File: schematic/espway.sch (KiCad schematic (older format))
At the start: 33 parts, among them J1 CONN_01X02, J2 CONN_01X02, J3 Conn_01x05_Male, SW1 SW_Push, U1 LM1117-3.3, U2 ESP-12E, U3 DRV8835, U4 LSM6DS3

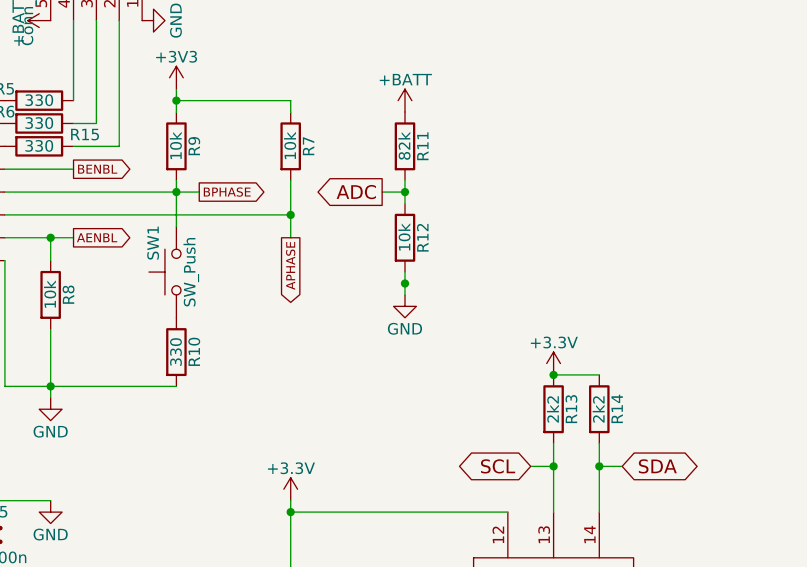
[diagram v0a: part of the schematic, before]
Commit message: Minor PCB track adjustments
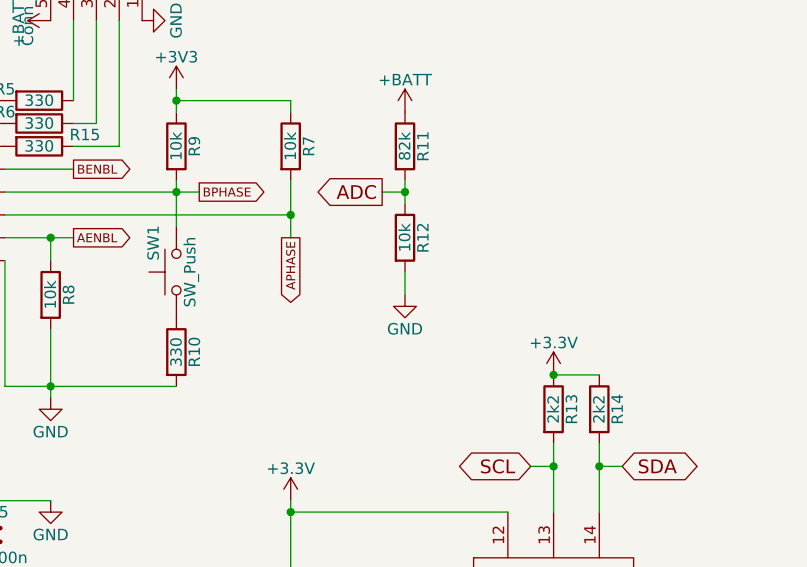
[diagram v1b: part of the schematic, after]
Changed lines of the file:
@@
 Wire Wire Line
 	10200 4650 10050 4650
-Connection ~ 8850 3150
 $Comp
 L R R9

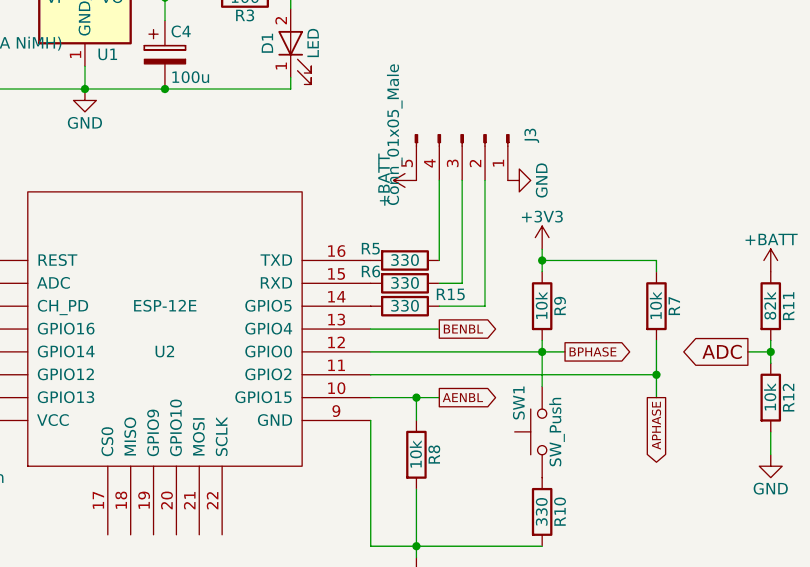
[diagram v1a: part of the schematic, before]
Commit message: Minor component value updates
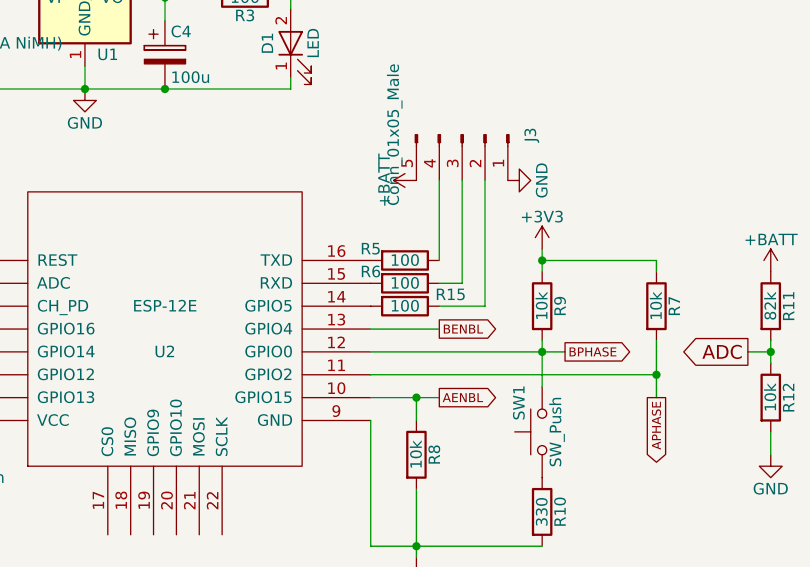
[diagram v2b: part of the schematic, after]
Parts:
- R15, R5, R6: value 330 -> 100
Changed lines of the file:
@@
 P 7250 2350
 F 0 "R5" V 7200 2200 50  0000 C CNN
-F 1 "330" V 7250 2350 50  0000 C CNN
+F 1 "100" V 7250 2350 50  0000 C CNN
 F 2 "Resistors_SMD:R_0603" V 7180 2350 50  0001 C CNN
 F 3 "" H 7250 2350 50  0001 C CNN
@@
 P 7250 2450
 F 0 "R6" V 7200 2300 50  0000 C CNN
-F 1 "330" V 7250 2450 50  0000 C CNN
+F 1 "100" V 7250 2450 50  0000 C CNN
 F 2 "Resistors_SMD:R_0603" V 7180 2450 50  0001 C CNN
 F 3 "" H 7250 2450 50  0001 C CNN
@@
 P 7250 2550
 F 0 "R15" V 7200 2750 50  0000 C CNN
-F 1 "330" V 7250 2550 50  0000 C CNN
+F 1 "100" V 7250 2550 50  0000 C CNN
 F 2 "Resistors_SMD:R_0603" V 7180 2550 50  0001 C CNN
 F 3 "" H 7250 2550 50  0001 C CNN
